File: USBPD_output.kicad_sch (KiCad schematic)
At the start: 6 parts, among them J3 USB-C_GCT_USB4105-GF-A, U6 TPS65987DDHRSHR

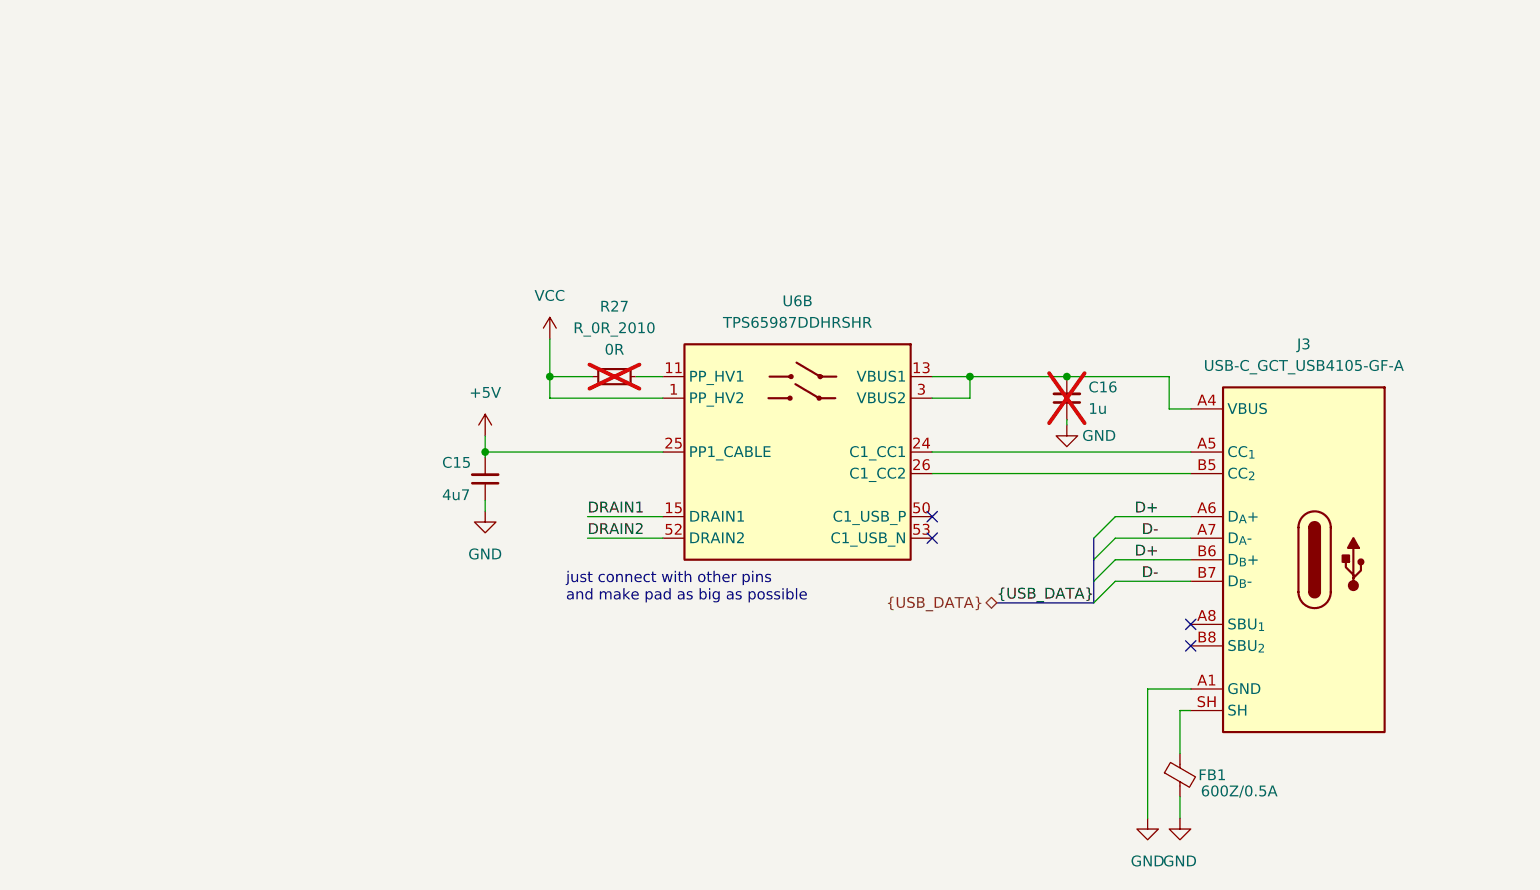
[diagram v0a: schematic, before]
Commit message: [#62623] Improve schematic, change 3V3 buck inductor, correct SPI, add testpoint
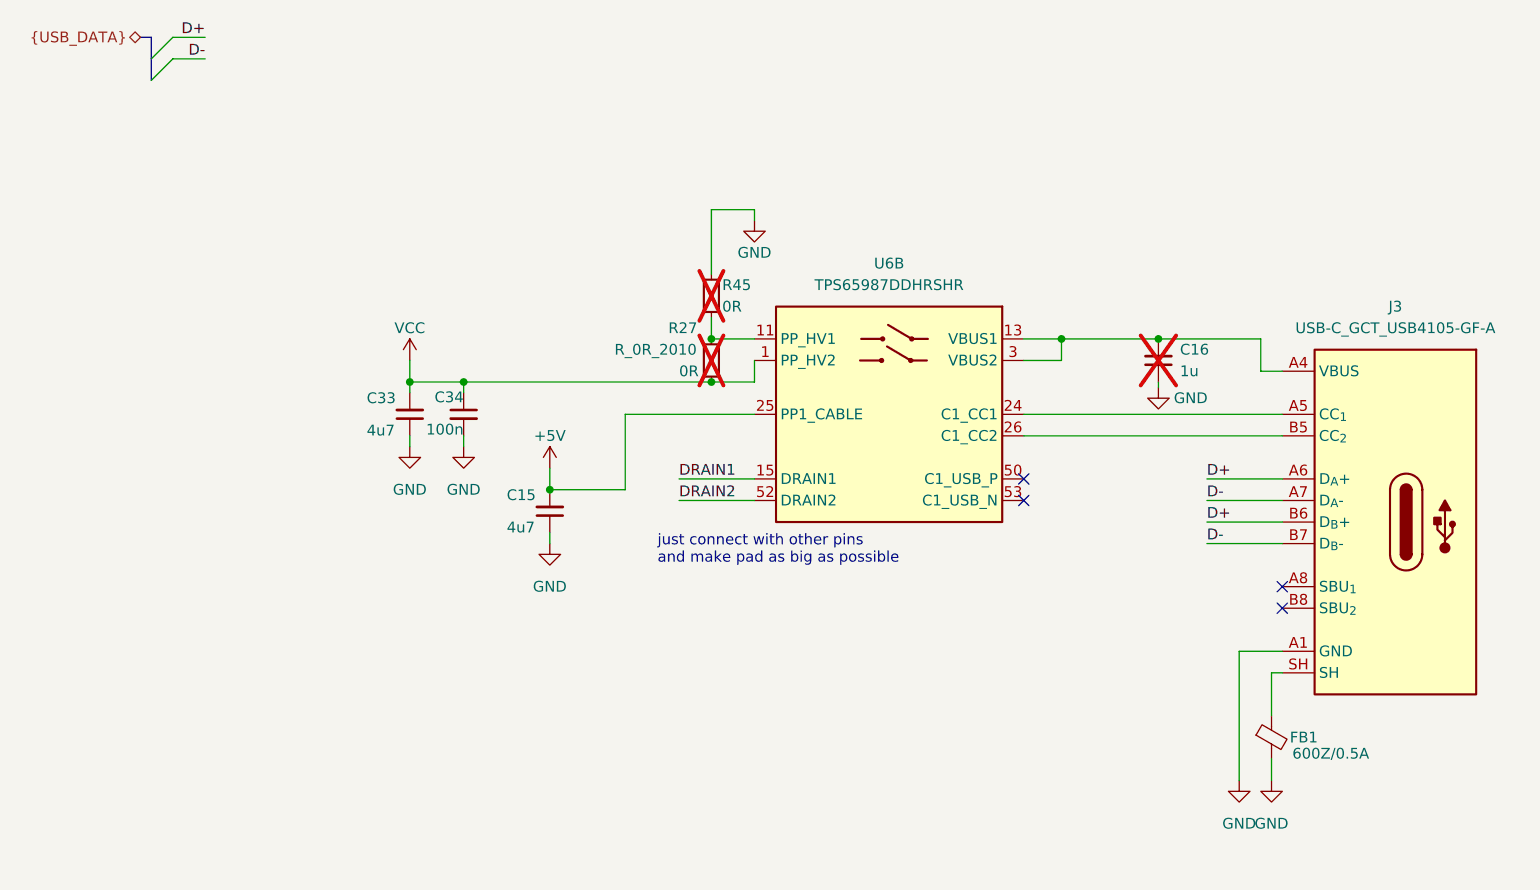
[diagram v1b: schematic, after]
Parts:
- added C33: C_4u7_25V_0402, antmicro-footprints:C_0402_1005Metric, symbol antmicroCapacitors0402:C_4u7_25V_0402
- added C34: C_100n_0402, antmicro-footprints:C_0402_1005Metric, symbol antmicroCapacitors0402:C_100n_0402
- added R45: R_0R_0402, antmicro-footprints:R_0402_1005Metric, symbol antmicroResistors0402:R_0R_0402
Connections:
- net GND: now also C33.1, C34.2, R45.2
- net VCC: now also C33.2, C34.1
- net at R27.2, U6.11 (PP_HV1): now also R45.1
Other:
- moved on the sheet: C15, C16, FB1, J3, R27, U6B

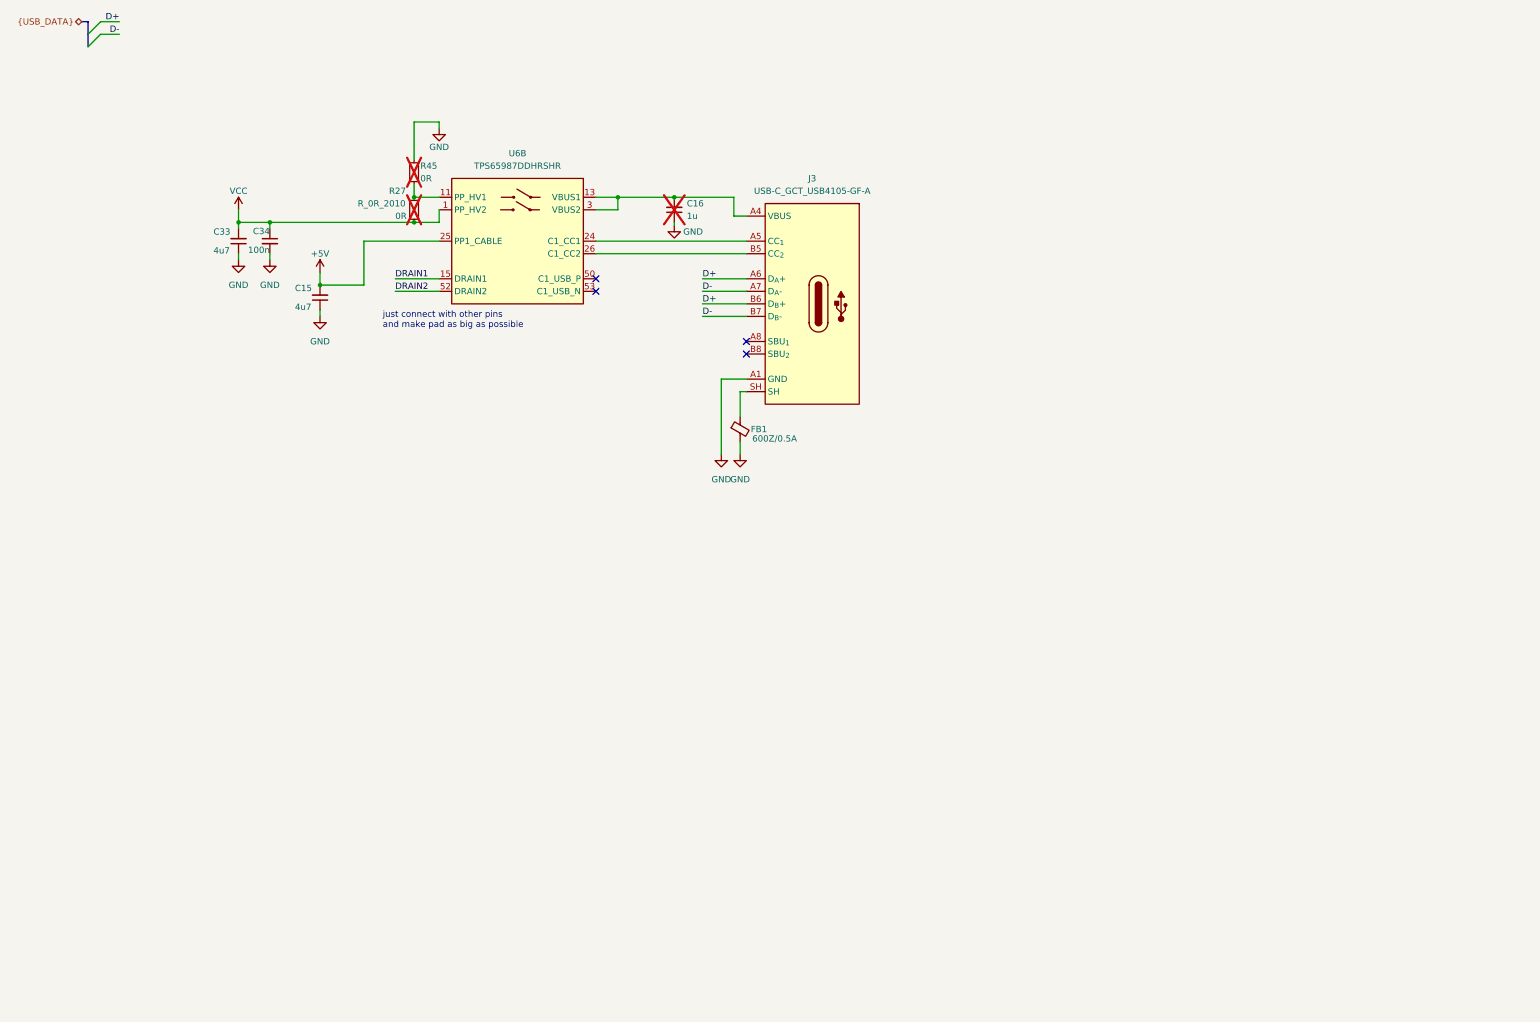
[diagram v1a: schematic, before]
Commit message: [#62623] Change hierarchy implementation
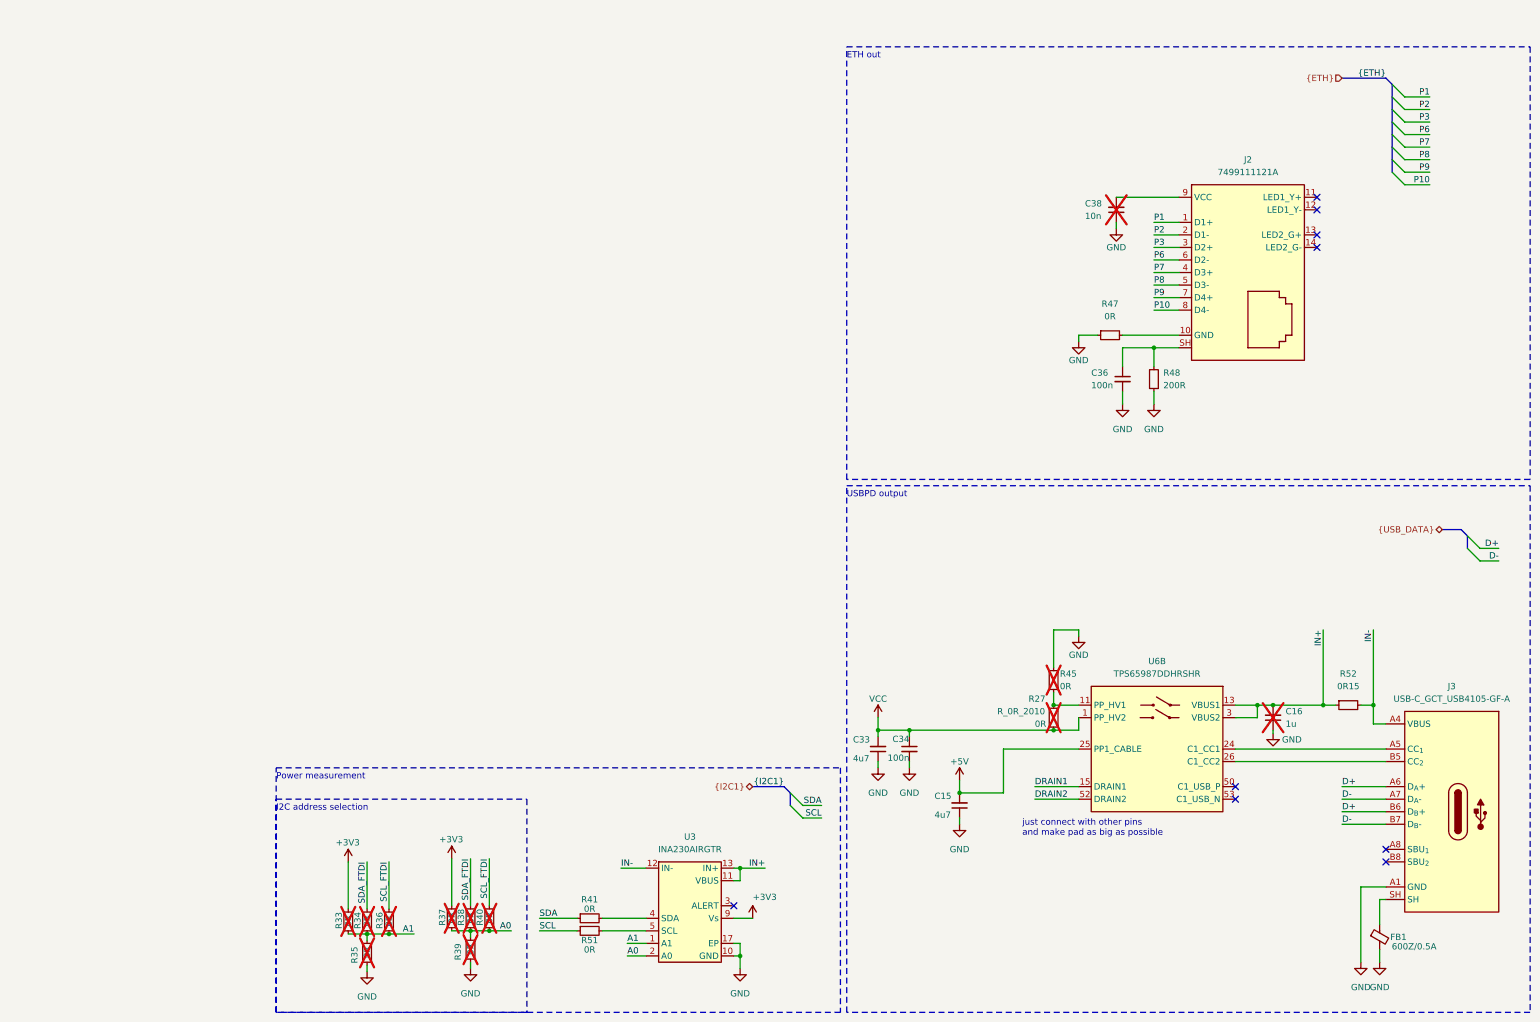
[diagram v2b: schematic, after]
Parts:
- added C36: C_100n_0402, antmicro-footprints:C_0402_1005Metric, symbol antmicroCapacitors0402:C_100n_0402
- added C38: C_10n_0603, antmicro-footprints:C_0603_1608Metric, symbol antmicroCapacitors0603:C_10n_0603
- added J2: Bus_RJ45_7499111121A, antmicro-footprints:RJ45_7499111121A_Horizontal, symbol antmicroModularConnectorsJacksWithMagnetics:Bus_RJ45_7499111121A
- added R33, R34, R35, R36, R37, R38, R39, R40, R41, R47, R51: R_0R_0402, antmicro-footprints:R_0402_1005Metric, symbol antmicroResistors0402:R_0R_0402
- added R48: R_200R_0402, antmicro-footprints:R_0402_1005Metric, symbol antmicroResistors0402:R_200R_0402
- added R52: R_0R15_2010, antmicro-footprints:R_2010_5025Metric, symbol antmicroResistorsmisc:R_0R15_2010
- added U3: INA230AIRGTR, antmicro-footprints:VQFN-16-1EP_3x3mm_P0.5mm_EP1.68x1.68mm, symbol antmicroPowerMeasurement:INA230AIRGTR
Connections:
- net GND: now also C36.2, C38.1, R35.1, R39.1, R47.1, R48.1, U3.10 (GND), U3.17 (EP)
- net IN-: now reaches J3.A4 (VBUS), J3.A9 (VBUS), J3.B4 (VBUS), J3.B9 (VBUS)
- net IN-: now also R52.2, U3.12 (IN-); no longer C16.2, U6.13 (VBUS1), U6.3 (VBUS2)
- new net: R41.2, U3.4 (SDA)
- new net: C36.1, J2.SH, R48.2
- new net: C38.2, J2.9 (VCC)
- new net: R51.2, U3.5 (SCL)
- new net: J2.10 (GND), R47.2
- new net: U3.14 (NC), U3.15 (NC), U3.16 (NC), U3.6 (NC), U3.7 (NC), U3.8 (NC)
- new net +3V3: R33.2, R37.2, U3.9 (Vs)
- new net A0: R37.1, R38.1, R39.2, R40.1, U3.2 (A0)
- new net A1: R33.1, R34.1, R35.2, R36.1, U3.1 (A1)
- new net IN+: C16.2, R52.1, U3.11 (VBUS), U3.13 (IN+), U6.13 (VBUS1), U6.3 (VBUS2)
- new net P1: J2.1 (D1+)
- new net P10: J2.8 (D4-)
- new net P2: J2.2 (D1-)
- new net P3: J2.3 (D2+)
- new net P6: J2.6 (D2-)
- new net P7: J2.4 (D3+)
- new net P8: J2.5 (D3-)
- new net P9: J2.7 (D4+)
- new net SCL: R51.1
- new net SCL_FTDI: R36.2, R40.2
- new net SDA: R41.1
- new net SDA_FTDI: R34.2, R38.2
- no-connect marks 4 -> 9
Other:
- note added: "ETH out"
- note added: "I2C address selection"
- note added: "Power measurement"
- note added: "USBPD output"
- moved on the sheet: C15, C16, C33, C34, FB1, J3, R27, R45, U6B

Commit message: [#62623] Minor changes in placement/schematic
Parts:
- removed R27: R_0R_2010, antmicro-footprints:R_2010_5025Metric, symbol antmicroResistorsmisc:R_0R_2010
- added R3: R_0R_22.4A_0603, antmicro-footprints:R_0603_1608Metric, symbol antmicroResistors0603:R_0R_22.4A_0603
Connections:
- net SCL_FTDI is gone; now on net SCL: R36.2, R40.2
- net SDA_FTDI is gone; now on net SDA: R34.2, R38.2
- net IN+: no longer U3.11 (VBUS)
- net IN-: now also U3.11 (VBUS)
- net VCC: now also R3.2
- net at R45.1, U6.11 (PP_HV1): now also R3.1
- now unconnected: U3.14 (NC), U3.15 (NC), U3.16 (NC), U3.6 (NC), U3.7 (NC), U3.8 (NC)

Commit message: [#62623] Las commit before major change in placement
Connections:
- net VCC renamed VBUS
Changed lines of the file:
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@@
+    )
+  )
+  (symbol (lib_id "antmicropower:VBUS") (at 200.66 181.61 0) (unit 1)
+    (in_bom yes) (on_board yes) (dnp no) (fields_autoplaced)
+    (property "Reference" "#PWR068" (at 200.66 185.42 0)
+      (effects (font (size 1.27 1.27)) hide)
+    )
+    (property "Value" "VBUS" (at 200.66 176.53 0)
+      (effects (font (size 1.27 1.27)))
+    )
+    (property "Footprint" "" (at 200.66 181.61 0)
+      (effects (font (size 1.27 1.27)) hide)
+    )
+    (property "Datasheet" "" (at 200.66 181.61 0)
+      (effects (font (size 1.27 1.27)) hide)
+    )
+    (pin "1")
+    (instances
+      (project "antmicro-poe-to-usbc-pd-adapter"
+        (path "/cf0d4429-3f03-449f-96a7-26d69371a46d/71fd6a9f-e91f-4e27-909c-676c68ed5a18"
+          (reference "#PWR068") (unit 1)
+        )
+      )
     )
   )
@@
         )
       )
-    )
-  )
-  (symbol (lib_id "antmicropower:VCC") (at 200.66 181.61 0) (unit 1)
-    (in_bom yes) (on_board yes) (dnp no)
-    (property "Reference" "#PWR068" (at 200.66 185.42 0)
-      (effects (font (size 1.27 1.27)) hide)
-    )
-    (property "Value" "VCC" (at 200.66 177.8 0)
-      (effects (font (size 1.27 1.27)))
-    )
-    (property "Footprint" "" (at 200.66 181.61 0)
-      (effects (font (size 1.27 1.27)) hide)
-    )
-    (property "Datasheet" "" (at 200.66 181.61 0)
-      (effects (font (size 1.27 1.27)) hide)
-    )
-    (pin "1")
-    (instances
-      (project "antmicro-poe-to-usbc-pd-adapter"
-        (path "/cf0d4429-3f03-449f-96a7-26d69371a46d/71fd6a9f-e91f-4e27-909c-676c68ed5a18"
-          (reference "#PWR068") (unit 1)
-        )
-      )
